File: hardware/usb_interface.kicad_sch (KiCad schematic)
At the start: 8 parts, among them J401 USB C 2.0

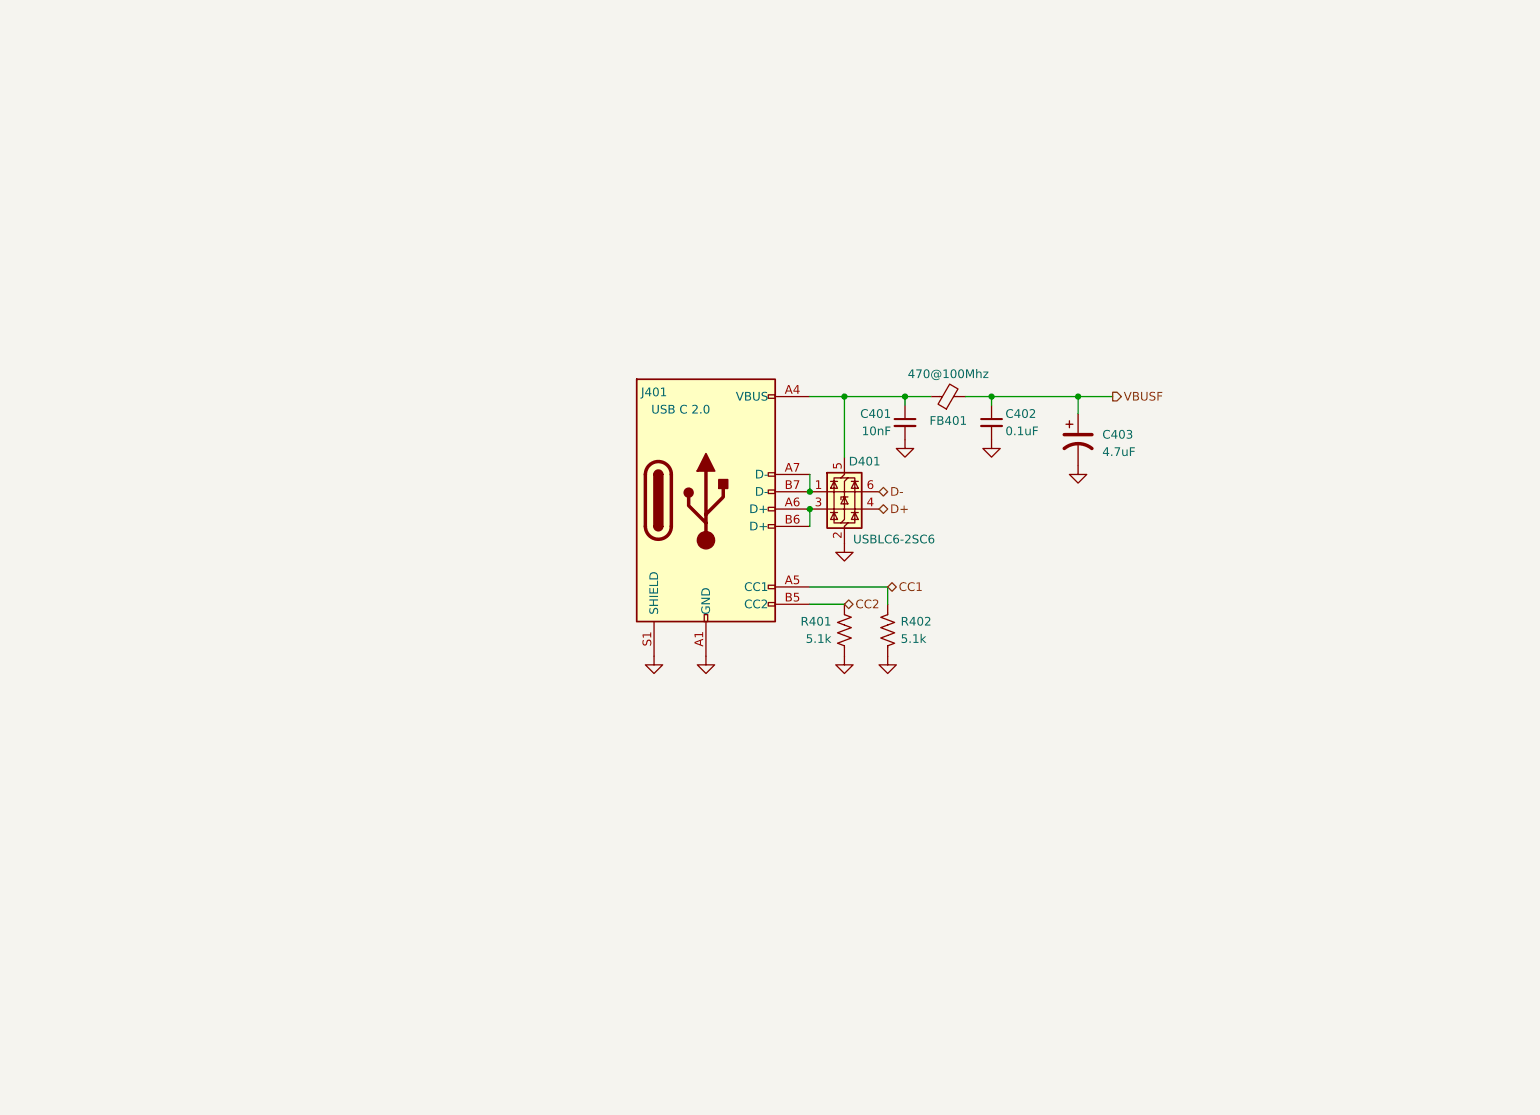
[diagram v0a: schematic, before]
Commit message: Finalize USB interface
Added soft-start
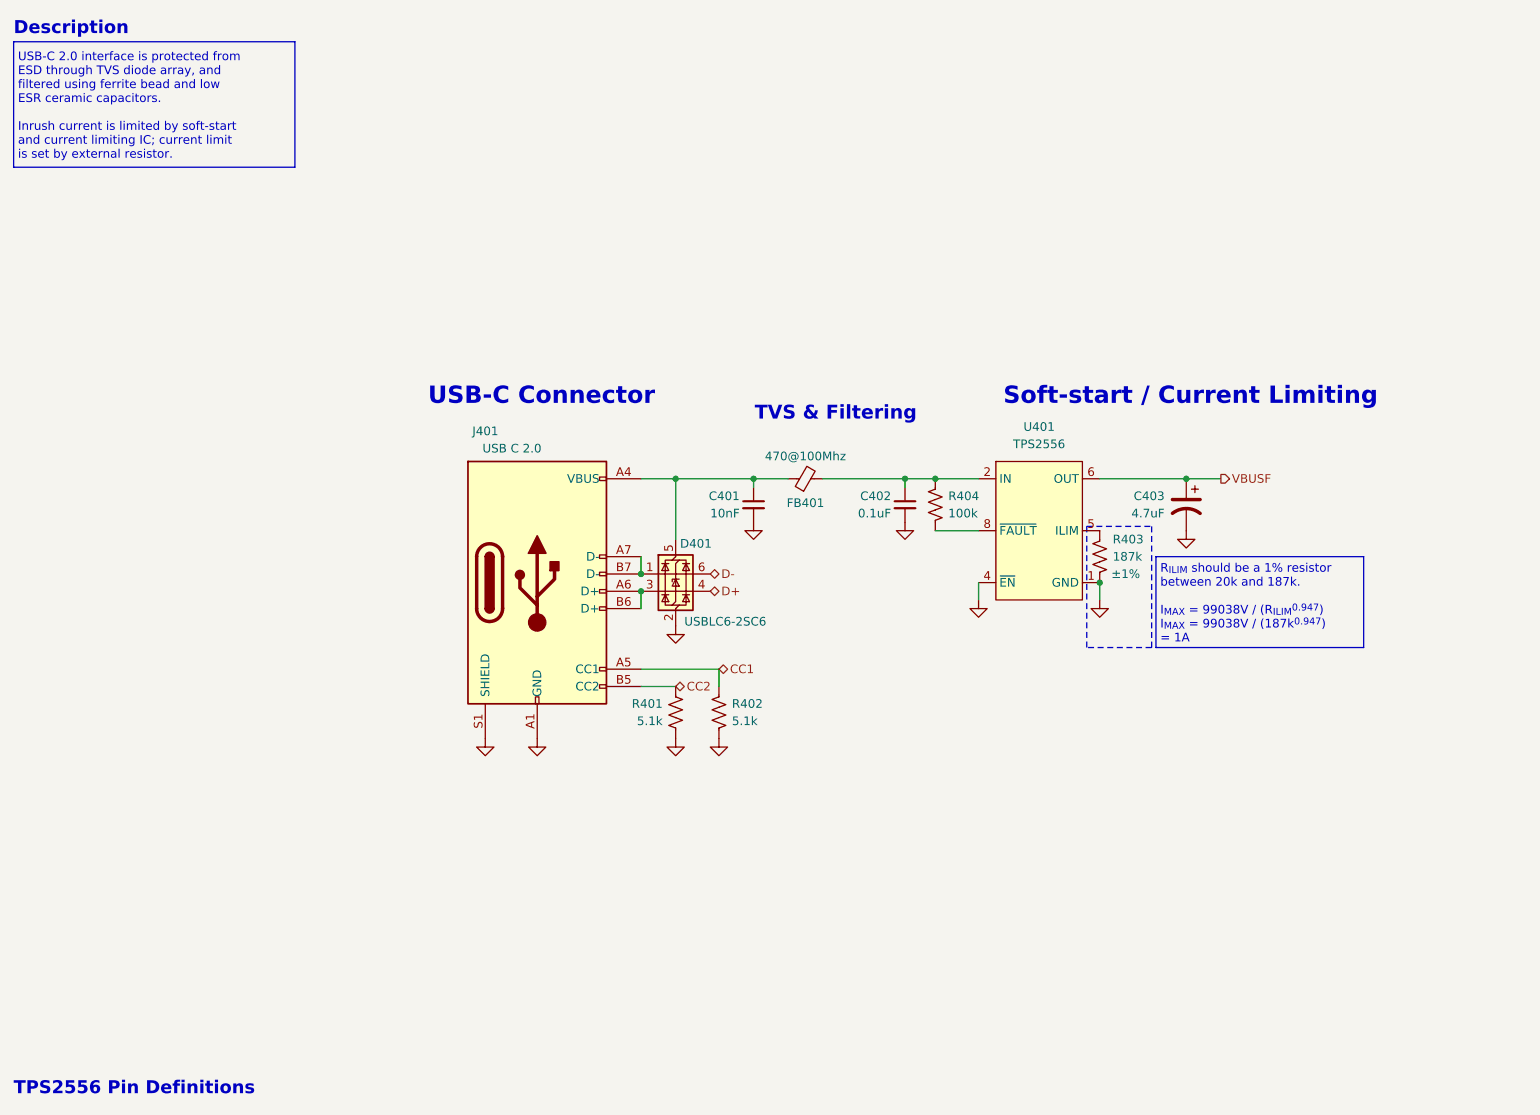
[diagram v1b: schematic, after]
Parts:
- added R403: 187k, symbol Device:R_US
- added R404: 100k, symbol Device:R_US
- added U401: TPS2556, carrier-wave:SON65P300X300X100-9N, symbol carrier-wave:TPS2556
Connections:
- net GND: now also R403.2, U401.1 (GND), U401.4 (~{EN}), U401.9 (PAD)
- net VBUSF: now also U401.6 (OUT), U401.7 (OUT); no longer C402.1, FB401.2
- new net: R404.2, U401.8 (~{FAULT})
- new net: R403.1, U401.5 (ILIM)
- new net IN: C402.1, FB401.2, R404.1, U401.2 (IN), U401.3 (IN)
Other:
- note added: "Description"
- note added: "R_{ILIM} should be a 1% resistor between 20k and 187k. I_{MAX} = 99038V / (R_{ILIM}^{0.947}) I_{MAX} = 99038V / (187k^{0.947}) = 1A"
- note added: "Soft-start / Current Limiting"
- note added: "TPS2556 Pin Definitions"
- note added: "TVS & Filtering"
- note added: "USB-C 2.0 interface is protected from ESD through TVS diode array, and filtered using ferrite bead and low ESR ceramic capacitors. Inrush current is limited by soft-start and current limiting IC; current limit is set by external resistor."
- note added: "USB-C Connector"
- moved on the sheet: C401, C402, C403, D401, FB401, J401, R401, R402

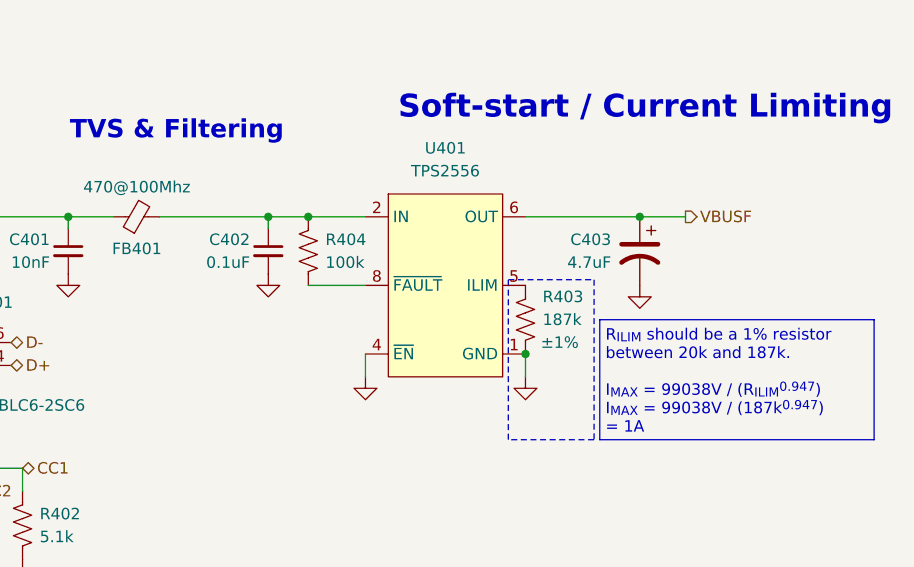
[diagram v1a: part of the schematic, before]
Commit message: Plan USB load switch replacement
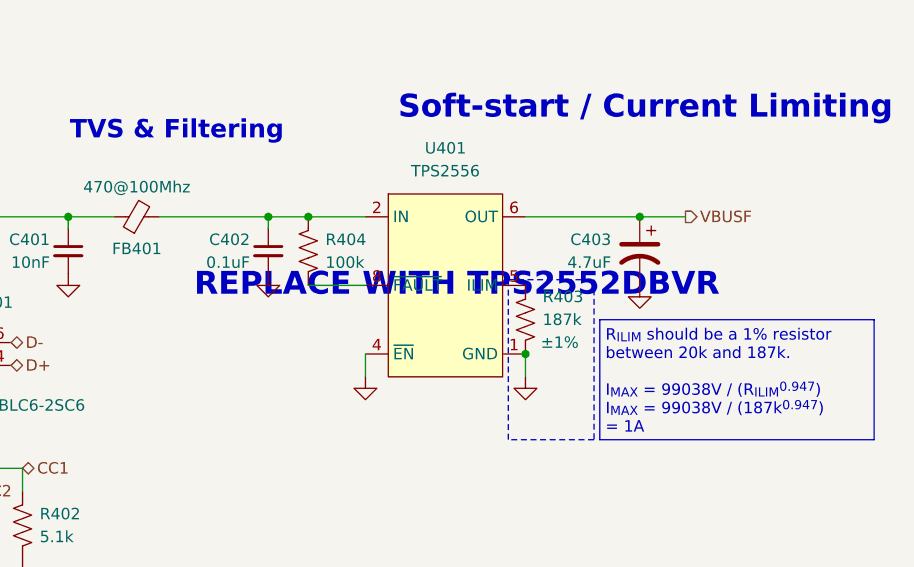
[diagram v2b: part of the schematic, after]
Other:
- note added: "REPLACE WITH TPS2552DBVR"
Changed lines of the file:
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@@
+		)
+	)
+	(text "REPLACE WITH TPS2552DBVR"
+		(exclude_from_sim no)
+		(at 164.465 88.265 0)
+		(effects
+			(font
+				(size 2.54 2.54)
+				(thickness 0.508)
+				(bold yes)
+				(color 255 0 0 1)
+			)
+			(href "https://www.ti.com/lit/ds/symlink/tps2552.pdf?HQS=dis-dk-null-digikeymode-dsf-pf-null-wwe&ts=1776891097277&ref_url=https%253A%252F%252Fwww.ti.com%252Fgeneral%252Fdocs%252Fsuppproductinfo.tsp%253FdistId%253D10%2526gotoUrl%253Dhttps%253A%252F%252Fwww.ti.com%252Flit%252Fgpn%252Ftps2552")
 		)
 	)

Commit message: Finalize power
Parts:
- removed U401: TPS2556, carrier-wave:SON65P300X300X100-9N, symbol carrier-wave:TPS2556
- added C404: 4.7uF, HIGHER ESR ELECTROLYTIC, symbol Device:C_Polarized_US
- added R405: 100k, symbol Device:R_US
- added R406: 4.7k, symbol Device:R_US
- added U401: TPS2552DBVR, Package_TO_SOT_SMD:SOT-23-6, symbol carrier-wave:TPS2552DBVR
- R403: value 187k -> 59k
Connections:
- net GND: now also C404.2, R406.2, U401.2 (GND)
- net ~{FAULT}: now reaches R404.2
- net ~{FAULT}: now also U401.4 (~{FAULT})
- net at R403.1: now also U401.5 (ILIM)
- net IN renamed VBUS_F
- net VBUS_F: now also C404.1, U401.1 (IN); no longer R404.1
- net VBUSF renamed VBUS_SW
- net VBUS_SW: now also U401.6 (OUT)
- new net +3.3VD: R404.1, R405.1
- new net ~{EN}: R405.2, R406.1, U401.3 (~{EN})
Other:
- note added: "Asymmetric voltage divider to drive ~{EN} below 0.66V threshold when manually enabled."
- note added: "Place filtering and IC close."
- note added: "R_{ILIM} should be a 1% resistor between 15k and 232k. I_{MAX} = 22980V / (R_{ILIM}^{0.94}) I_{MAX} = 22980V / (59k^{0.94}) = 500mA"
- note added: "TPS2552 Pin Definitions"
- note added: "USB-C 2.0 connection is protected against ESD through TVS diode array, and filtered using a ferrite bead and low-ESR ceramic capacitors. A dedicated load switch IC with built-in soft-start and programmable current limiting ensures 500mA USB spec, and limits inrush. VBUSF is exposed before the load switch, allowing an MCU to remain operational during power faults. The ~{FAULT} output of the load s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"
- note removed: "REPLACE WITH TPS2552DBVR"
- note removed: "R_{ILIM} should be a 1% resistor between 20k and 187k. I_{MAX} = 99038V / (R_{ILIM}^{0.947}) I_{MAX} = 99038V / (187k^{0.947}) = 1A"
- note removed: "TPS2556 Pin Definitions"
- note removed: "USB-C 2.0 interface is protected from ESD through TVS diode array, and filtered using ferrite bead and low ESR ceramic capacitors. Inrush current is limited by soft-start and current limiting IC; current limit is set by external resistor."
- moved on the sheet: C401, C403, D401, FB401, J401, R401, R402, R403, R404

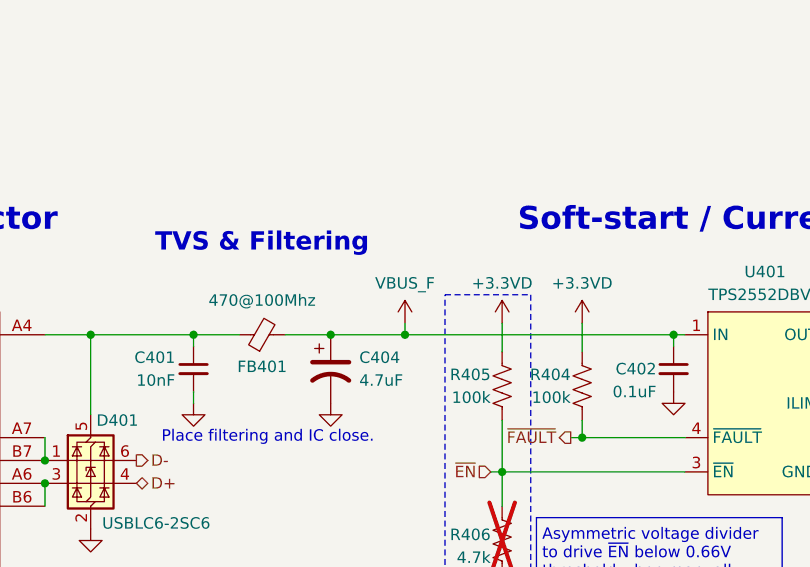
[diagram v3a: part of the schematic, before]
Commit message: Rename VBUS_F to VBUS
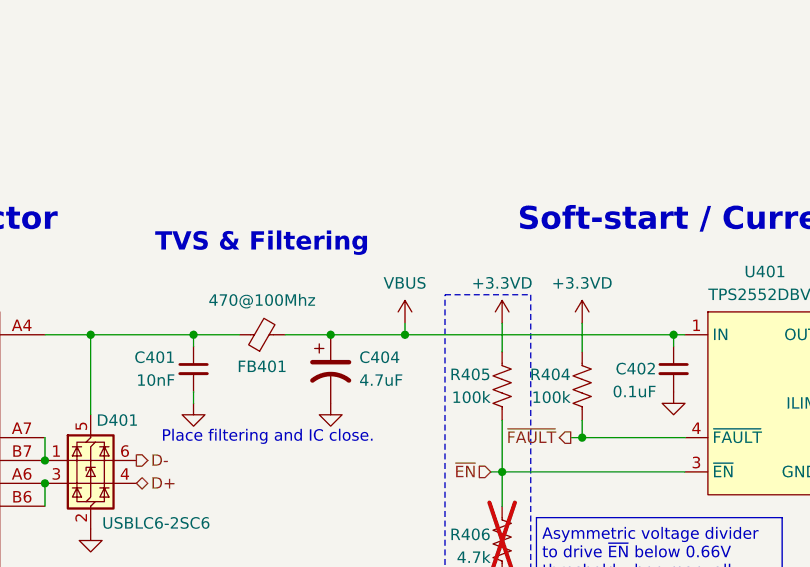
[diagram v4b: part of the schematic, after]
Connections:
- net VBUS_F renamed VBUS
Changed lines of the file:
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@@
 			)
 		)
-		(property "Value" "VBUS_F"
+		(property "Value" "VBUS"
 			(at 131.445 78.105 0)
 			(show_name no)
